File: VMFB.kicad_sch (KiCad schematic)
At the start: 112 parts, among them J1 Barrel_Jack_Switch, J10 Conn_01x03_Pin, J11 Conn_01x06_Pin, J12 Conn_01x04_Pin, J13 Conn_01x04_Pin, J14 Conn_01x04_Pin, J2 USB_B, J3 Screw_Terminal_01x02, J4 Screw_Terminal_01x03, J5 Conn_01x03_Pin, J6 Conn_01x04_Pin, J7 Conn_01x04_Pin, J8 Conn_01x04_Pin, J9 Conn_01x02_Pin, Q1 BC547, Q2 BC547, Q3 BC547, Q4 BD139, Q5 TIP41C, Q6 BC547, U1 LM358, U2 NE555P, U3 NE555P, U4 NE555P, U5 NE555P

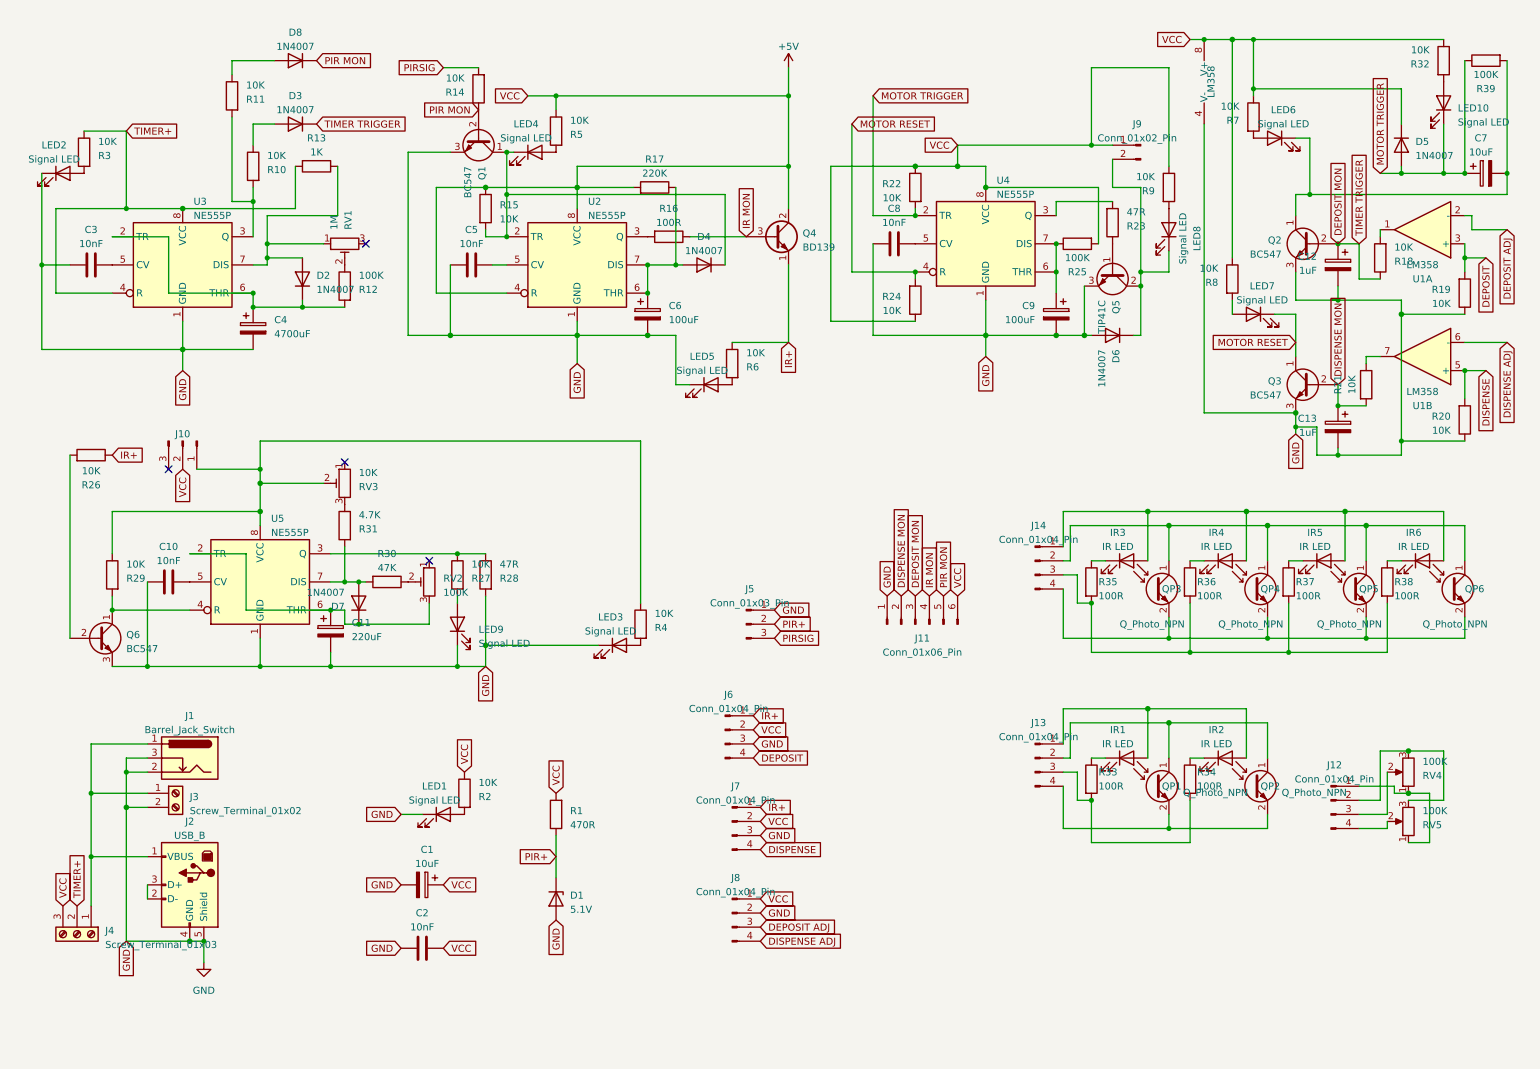
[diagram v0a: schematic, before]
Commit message: added monitoring-only header, moved IR LED switch transistor from VCC to GND and removed a pin from the sensor headers (no need for separate VCC for the IR LEDS), 100R to 47R on Q$ base, 47R to 22R on Q5 base
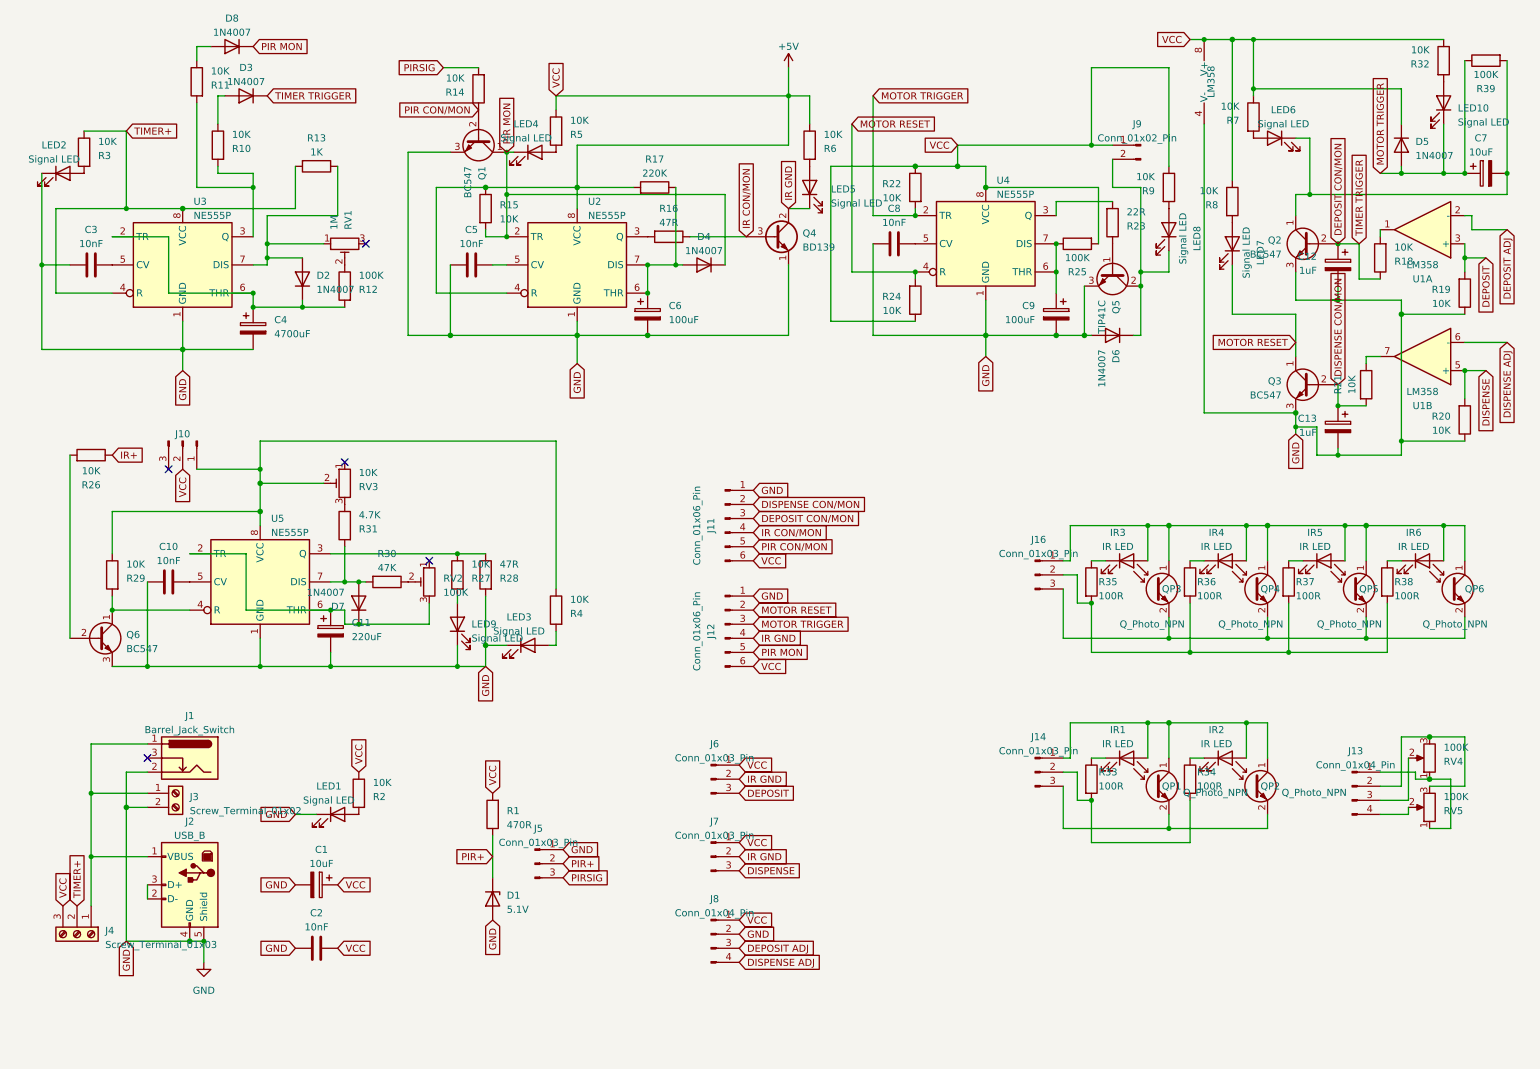
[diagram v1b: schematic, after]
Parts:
- removed J13, J14, J6, J7: Conn_01x04_Pin, Connector_PinHeader_2.54mm:PinHeader_1x04_P2.54mm_Vertical, symbol Connector:Conn_01x04_Pin
- added J12: Conn_01x06_Pin, Connector_PinHeader_2.54mm:PinHeader_1x06_P2.54mm_Vertical, symbol Connector:Conn_01x06_Pin
- added J14, J16, J6, J7: Conn_01x03_Pin, Connector_PinHeader_2.54mm:PinHeader_1x03_P2.54mm_Vertical, symbol Connector:Conn_01x03_Pin
- R16: value 100R -> 47R; footprint Resistor_THT:R_Axial_DIN0207_L6.3mm_D2.5mm_P2.54mm_Vertical -> Resistor_THT:R_Axial_DIN0309_L9.0mm_D3.2mm_P2.54mm_Vertical
- R23: value 47R -> 22R
- renumbered J12 to J13
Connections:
- net +5V: now also R6.1, J12.6 (Pin_6), J6.1 (Pin_1), J7.1 (Pin_1); no longer Q4.2 (C)
- net DEPOSIT: now also J6.3 (Pin_3)
- net DISPENSE: now also J7.3 (Pin_3)
- net GND: now also Q4.1 (E), J12.1 (Pin_1); no longer J1.3, LED5.1 (K)
- net IR+: no longer Q4.1 (E), R6.1
- net MOTOR RESET: now also J12.2 (Pin_2)
- net MOTOR TRIGGER: now also J12.3 (Pin_3)
- net PIR MON: now also D4.1 (K), LED4.1 (K), Q1.1 (C), R15.2, U2.2 (TR), J12.5 (Pin_5); no longer J11.5 (Pin_5), Q1.2 (B), R14.1
- net at IR1.2 (A), IR2.2 (A): now also QP1.1 (C), QP2.1 (C), J14.1 (Pin_1)
- net at IR3.2 (A), IR4.2 (A), IR5.2 (A)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: now also QP3.1 (C), QP4.1 (C), QP5.1 (C), QP6.1 (C), J16.1 (Pin_1)
- net at R35.2, R36.2, R37.2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: now also J16.2 (Pin_2)
- net at QP3.2 (E), QP4.2 (E), QP5.2 (E)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: now also J16.3 (Pin_3)
- net at R33.2, R34.2: now also J14.2 (Pin_2)
- net at QP1.2 (E), QP2.2 (E): now also J14.3 (Pin_3)
- net DEPOSIT MON renamed DEPOSIT CON/MON
- net DISPENSE MON renamed DISPENSE CON/MON
- net IR MON renamed IR CON/MON
- new net IR GND: J12.4 (Pin_4), J6.2 (Pin_2), J7.2 (Pin_2), LED5.1 (K), Q4.2 (C)
- new net PIR CON/MON: J11.5 (Pin_5), Q1.2 (B), R14.1
- no-connect marks 4 -> 5
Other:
- moved on the sheet: C1, C2, D1, D3, D8, J11, J13, J5, J8, LED1, LED3, LED7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

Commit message: moved dispense monitoring directly to the collector of Q2 so you can tell if it's jammed
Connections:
- net IR+ is gone; now on net IR CON/MON: R26.1
- net MOTOR TRIGGER: no longer J12.3 (Pin_3)
- net DEPOSIT MON: now reaches C7.2, LED6.1 (K), Q2.1 (C), R39.2
- net DEPOSIT MON: now also J12.3 (Pin_3)
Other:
- moved on the sheet: J10
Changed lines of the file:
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@@
   )
   (no_connect (at 87.63 111.76))
-  (no_connect (at 40.64 95.25))
+  (no_connect (at 48.26 95.25))
   (no_connect (at 72.39 93.98))
   (no_connect (at 36.83 147.32))
@@
     (stroke (width 0) (type default))
   )
-  (wire (pts (xy 45.72 95.25) (xy 57.15 95.25))
+  (wire (pts (xy 53.34 95.25) (xy 57.15 95.25))
     (stroke (width 0) (type default) (color 221 119 0 1))
   )
@@
     )
   )
-  (global_label "MOTOR TRIGGER" (shape input) (at 146.05 123.19 0) (fields_autoplaced)
+  (global_label "DEPOSIT MON" (shape input) (at 146.05 123.19 0) (fields_autoplaced)
     (effects (font (size 1.27 1.27)) (justify left))
-    (property "Intersheetrefs" "${INTERSHEET_REFS}" (at 164.0748 123.19 0) (show_name)
+    (property "Intersheetrefs" "${INTERSHEET_REFS}" (at 161.8372 123.19 0) (show_name)
       (effects (font (size 1.27 1.27)) (justify left) hide)
     )
@@
     )
   )
-  (global_label "VCC" (shape input) (at 43.18 95.25 270) (fields_autoplaced)
+  (global_label "VCC" (shape input) (at 50.8 95.25 270) (fields_autoplaced)
     (effects (font (size 1.27 1.27)) (justify right))
-    (property "Intersheetrefs" "${INTERSHEET_REFS}" (at 43.18 101.7844 90) (show_name)
+    (property "Intersheetrefs" "${INTERSHEET_REFS}" (at 50.8 101.7844 90) (show_name)
       (effects (font (size 1.27 1.27)) (justify right) hide)
     )
@@
     )
   )
+  (global_label "DEPOSIT MON" (shape input) (at 243.84 45.72 180) (fields_autoplaced)
+    (effects (font (size 1.27 1.27)) (justify right))
+    (property "Intersheetrefs" "${INTERSHEET_REFS}" (at 228.0528 45.72 0) (show_name)
+      (effects (font (size 1.27 1.27)) (justify right) hide)
+    )
+  )
   (global_label "MOTOR RESET" (shape input) (at 243.84 72.39 180) (fields_autoplaced)
     (effects (font (size 1.27 1.27)) (justify right))
@@
     )
   )
-  (global_label "IR+" (shape input) (at 30.48 92.71 0) (fields_autoplaced)
+  (global_label "IR CON{slash}MON" (shape input) (at 30.48 92.71 0) (fields_autoplaced)
     (effects (font (size 1.27 1.27)) (justify left))
-    (property "Intersheetrefs" "${INTERSHEET_REFS}" (at 36.833 92.71 0) (show_name)
+    (property "Intersheetrefs" "${INTERSHEET_REFS}" (at 45.6021 92.71 0) (show_name)
       (effects (font (size 1.27 1.27)) (justify left) hide)
     )
@@
     )
   )
-  (symbol (lib_id "Connector:Conn_01x03_Pin") (at 43.18 90.17 270) (unit 1)
+  (symbol (lib_id "Connector:Conn_01x03_Pin") (at 50.8 90.17 270) (unit 1)
     (in_bom yes) (on_board yes) (dnp no) (fields_autoplaced)
-    (property "Reference" "J10" (at 43.18 88.9 90)
+    (property "Reference" "J10" (at 50.8 88.9 90)
       (effects (font (size 1.27 1.27)))
     )
-    (property "Value" "Conn_01x03_Pin" (at 46.99 90.805 0)
+    (property "Value" "Conn_01x03_Pin" (at 54.61 90.805 0)
       (effects (font (size 1.27 1.27)) hide)
     )
-    (property "Footprint" "Connector_PinHeader_2.54mm:PinHeader_1x03_P2.54mm_Vertical" (at 43.18 90.17 0)
+    (property "Footprint" "Connector_PinHeader_2.54mm:PinHeader_1x03_P2.54mm_Vertical" (at 50.8 90.17 0)
       (effects (font (size 1.27 1.27)) hide)
     )
-    (property "Datasheet" "~" (at 43.18 90.17 0)
+    (property "Datasheet" "~" (at 50.8 90.17 0)
       (effects (font (size 1.27 1.27)) hide)
     )

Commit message: updated version to 1.3
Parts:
- Q1, Q2, Q3, Q6: footprint Package_TO_SOT_THT:TO-92_Inline -> Package_TO_SOT_THT:TO-92_Inline_Wide
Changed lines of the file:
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@@
       (effects (font (size 1.27 1.27)) (justify left))
     )
-    (property "Footprint" "Package_TO_SOT_THT:TO-92_Inline" (at 33.02 127.635 0)
+    (property "Footprint" "Package_TO_SOT_THT:TO-92_Inline_Wide" (at 33.02 127.635 0)
       (effects (font (size 1.27 1.27) italic) (justify left) hide)
     )
@@
       (effects (font (size 1.27 1.27)) (justify left))
     )
-    (property "Footprint" "Package_TO_SOT_THT:TO-92_Inline" (at 94.615 40.64 0)
+    (property "Footprint" "Package_TO_SOT_THT:TO-92_Inline_Wide" (at 94.615 40.64 0)
       (effects (font (size 1.27 1.27) italic) (justify left) hide)
     )
@@
       (effects (font (size 1.27 1.27)) (justify left))
     )
-    (property "Footprint" "Package_TO_SOT_THT:TO-92_Inline" (at 241.3 81.915 0)
+    (property "Footprint" "Package_TO_SOT_THT:TO-92_Inline_Wide" (at 241.3 81.915 0)
       (effects (font (size 1.27 1.27) italic) (justify left) hide)
     )
@@
       (effects (font (size 1.27 1.27)) (justify left))
     )
-    (property "Footprint" "Package_TO_SOT_THT:TO-92_Inline" (at 241.3 56.515 0)
+    (property "Footprint" "Package_TO_SOT_THT:TO-92_Inline_Wide" (at 241.3 56.515 0)
       (effects (font (size 1.27 1.27) italic) (justify left) hide)
     )

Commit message: added LDR-based light sensor to turn off timed dispense when the sun sets
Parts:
- added J16, J17: Conn_01x03_Pin, Connector_PinHeader_2.54mm:PinHeader_1x03_P2.54mm_Vertical, symbol Connector:Conn_01x03_Pin
- added LDR1: GL5549, OptoDevice:R_LDR_5.1x4.3mm_P3.4mm_Vertical, symbol Sensor_Optical:LDR07
- added R41: 470, Resistor_THT:R_Axial_DIN0207_L6.3mm_D2.5mm_P2.54mm_Vertical, symbol Device:R
- added RV6: 25K, Potentiometer_THT:Potentiometer_Piher_PT-10-V10_Vertical, symbol Device:R_Potentiometer
- renumbered J16 to J15
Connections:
- net GND: now also J17.3 (Pin_3)
- net TIMER+: now also J17.1 (Pin_1); no longer U3.4 (R)
- new net: J16.1 (Pin_1), R41.1
- new net: LDR1.1, R41.2
- new net: J17.2 (Pin_2), U3.4 (R)
- new net: J16.2 (Pin_2), LDR1.2, RV6.2
- new net: J16.3 (Pin_3), RV6.3
- no-connect marks 5 -> 6

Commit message: improvements to the daytimer, and added an LED so you can see the status
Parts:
- removed J16: Conn_01x03_Pin, Connector_PinHeader_2.54mm:PinHeader_1x03_P2.54mm_Vertical, symbol Connector:Conn_01x03_Pin
- added J18: Conn_01x02_Pin, Connector_PinHeader_2.54mm:PinHeader_1x02_P2.54mm_Vertical, symbol Connector:Conn_01x02_Pin
- added LED11: Signal LED, LED_THT:LED_D5.0mm, symbol Device:LED
- added Q7: BC547, Package_TO_SOT_THT:TO-92_Inline_Wide, symbol Transistor_BJT:BC547
- added R40, R42: 10K, Resistor_THT:R_Axial_DIN0207_L6.3mm_D2.5mm_P2.54mm_Vertical, symbol Device:R
- R12: value 100K -> 220K
- RV1: value 1M -> 2M
- RV6: value 25K -> 10K
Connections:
- net GND: now also RV6.3, Q7.3 (E)
- net TIMER+: now also R40.2, R42.1
- net at R41.1: now also J18.1 (Pin_1)
- net at U3.4 (R): now also LED11.1 (K), Q7.1 (C), R40.1; no longer J17.2 (Pin_2)
- net at RV6.2: now also J17.2 (Pin_2), Q7.2 (B); no longer LDR1.2
- new net: J18.2 (Pin_2), LDR1.2
- new net: LED11.2 (A), R42.2
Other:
- moved on the sheet: J17

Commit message: minor adjustments to the daytimer
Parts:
- added R43: 470R, Resistor_THT:R_Axial_DIN0207_L6.3mm_D2.5mm_P2.54mm_Vertical, symbol Device:R
- R40: value 10K -> 22K
- RV6: value 10K -> 25K
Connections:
- net at J17.2 (Pin_2), Q7.2 (B): now also R43.1; no longer RV6.2
- new net: R43.2, RV6.2
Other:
- moved on the sheet: RV6
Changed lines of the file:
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@@
   (junction (at 246.38 45.72) (diameter 0) (color 0 0 0 0)
   )
-  (junction (at 29.21 83.82) (diameter 0) (color 0 0 0 0)
-  )
   (junction (at 200.66 54.61) (diameter 0) (color 0 0 0 0)
   )
@@
   (junction (at 242.57 128.27) (diameter 0) (color 0 0 0 1)
   )
+  (junction (at 35.56 83.82) (diameter 0) (color 0 0 0 0)
+  )
   (junction (at 224.79 128.27) (diameter 0) (color 0 0 0 1)
   )
+  (junction (at 21.59 80.01) (diameter 0) (color 0 0 0 0)
+  )
   (junction (at 200.66 59.69) (diameter 0) (color 0 0 0 0)
   )
@@
   (junction (at 238.76 125.73) (diameter 0) (color 0 255 0 1)
   )
-  (junction (at 25.4 80.01) (diameter 0) (color 0 0 0 0)
-  )
   (junction (at 92.71 110.49) (diameter 0) (color 0 0 0 0)
   )
@@
   (no_connect (at 87.63 111.76))
   (no_connect (at 48.26 95.25))
-  (no_connect (at 29.21 76.2))
+  (no_connect (at 35.56 76.2))
   (no_connect (at 72.39 93.98))
   (no_connect (at 36.83 147.32))
@@
     (stroke (width 0) (type default))
   )
-  (wire (pts (xy 20.32 81.28) (xy 25.4 81.28))
+  (wire (pts (xy 20.32 81.28) (xy 21.59 81.28))
     (stroke (width 0) (type default))
   )
@@
     (stroke (width 0) (type default) (color 194 0 0 1))
   )
+  (wire (pts (xy 35.56 83.82) (xy 29.21 83.82))
+    (stroke (width 0) (type default))
+  )
   (wire (pts (xy 236.22 17.78) (xy 236.22 26.67))
     (stroke (width 0) (type default) (color 194 0 0 1))
@@
     (stroke (width 0) (type default))
   )
-  (wire (pts (xy 29.21 83.82) (xy 39.37 83.82))
-    (stroke (width 0) (type default))
-  )
   (wire (pts (xy 191.77 129.54) (xy 191.77 132.08))
     (stroke (width 0) (type default))
@@
     (stroke (width 0) (type default) (color 0 0 0 1))
   )
+  (wire (pts (xy 21.59 80.01) (xy 21.59 81.28))
+    (stroke (width 0) (type default))
+  )
   (wire (pts (xy 251.46 91.44) (xy 251.46 92.71))
     (stroke (width 0) (type default))
@@
     (stroke (width 0) (type default))
   )
+  (wire (pts (xy 35.56 83.82) (xy 39.37 83.82))
+    (stroke (width 0) (type default))
+  )
   (wire (pts (xy 55.88 41.91) (xy 55.88 44.45))
     (stroke (width 0) (type default))
@@
     (stroke (width 0) (type default))
   )
-  (wire (pts (xy 25.4 81.28) (xy 25.4 80.01))
-    (stroke (width 0) (type default))
-  )
   (wire (pts (xy 243.84 87.63) (xy 243.84 88.9))
     (stroke (width 0) (type default) (color 0 0 0 1))
@@
     (stroke (width 0) (type default) (color 255 0 0 1))
   )
-  (wire (pts (xy 25.4 73.66) (xy 25.4 80.01))
+  (wire (pts (xy 21.59 73.66) (xy 21.59 80.01))
     (stroke (width 0) (type default))
   )
@@
     (stroke (width 0) (type default))
   )
-  (wire (pts (xy 31.75 73.66) (xy 25.4 73.66))
+  (wire (pts (xy 31.75 73.66) (xy 21.59 73.66))
     (stroke (width 0) (type default))
   )
@@
     (stroke (width 0) (type default) (color 0 0 0 1))
   )
+  (wire (pts (xy 21.59 80.01) (xy 24.13 80.01))
+    (stroke (width 0) (type default))
+  )
   (wire (pts (xy 110.49 90.17) (xy 110.49 116.84))
     (stroke (width 0) (type default) (color 221 119 0 1))
@@
       (effects (font (size 1.27 1.27)) (justify right))
     )
-    (property "Value" "10K" (at 22.86 65.405 0)
+    (property "Value" "22K" (at 22.86 65.405 0)
       (effects (font (size 1.27 1.27)) (justify right))
     )
@@
     )
   )
-  (symbol (lib_id "Device:R_Potentiometer") (at 29.21 80.01 0) (mirror y) (unit 1)
+  (symbol (lib_id "Device:R_Potentiometer") (at 35.56 80.01 0) (mirror y) (unit 1)
     (in_bom yes) (on_board yes) (dnp no)
-    (property "Reference" "RV6" (at 33.02 80.01 90)
+    (property "Reference" "RV6" (at 39.37 80.01 90)
       (effects (font (size 1.27 1.27)))
     )
-    (property "Value" "10K" (at 35.56 80.01 90)
+    (property "Value" "25K" (at 41.91 80.01 90)
       (effects (font (size 1.27 1.27)))
     )
-    (property "Footprint" "Potentiometer_THT:Potentiometer_Piher_PT-10-V10_Vertical" (at 29.21 80.01 0)
+    (property "Footprint" "Potentiometer_THT:Potentiometer_Piher_PT-10-V10_Vertical" (at 35.56 80.01 0)
       (effects (font (size 1.27 1.27)) hide)
     )
-    (property "Datasheet" "~" (at 29.21 80.01 0)
+    (property "Datasheet" "~" (at 35.56 80.01 0)
       (effects (font (size 1.27 1.27)) hide)
     )
@@
         )
       )
+    )
+  )
+  (symbol (lib_id "Device:R") (at 27.94 80.01 90) (unit 1)
+    (in_bom yes) (on_board yes) (dnp no)
+    (property "Reference" "R43" (at 28.575 82.55 0)
+      (effects (font (size 1.27 1.27)) (justify right))
+    )
+    (property "Value" "470R" (at 26.035 82.55 0)
+      (effects (font (size 1.27 1.27)) (justify right))
+    )
+    (property "Footprint" "Resistor_THT:R_Axial_DIN0207_L6.3mm_D2.5mm_P2.54mm_Vertical" (at 27.94 81.788 90)
+      (effects (font (size 1.27 1.27)) hide)
+    )
+    (property "Datasheet" "~" (at 27.94 80.01 0)
+      (effects (font (size 1.27 1.27)) hide)
+    )
+    (pin "1")
+    (pin "2")
+    (instances
+      (project "VMFB"
+        (path "/840789ee-60d4-4003-8113-c1b030a45492"
+          (reference "R43") (unit 1)
+        )
+      )

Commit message: more adjustments to the daytimer
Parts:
- removed J13, J8: Conn_01x04_Pin, Connector_PinHeader_2.54mm:PinHeader_1x04_P2.54mm_Vertical, symbol Connector:Conn_01x04_Pin
- RV4, RV5: footprint Potentiometer_THT:Potentiometer_Piher_T-16H_Single_Horizontal -> Potentiometer_THT:Potentiometer_Piher_PT-10-V10_Vertical
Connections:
- net +5V: now also R32.2, RV4.3, RV5.1; no longer R32.1
- net DEPOSIT ADJ: now also RV4.2
- net DISPENSE ADJ: now also RV5.2
- net GND: now also J17.2 (Pin_2), RV4.1, RV5.3; no longer J17.3 (Pin_3), RV6.3
- net TIMER+: now also RV6.1; no longer J17.1 (Pin_1)
- net at LED10.2 (A): now also R32.1; no longer R32.2
- net at R41.1: now also LDR1.2; no longer J18.1 (Pin_1)
- net at R41.2: now also J18.1 (Pin_1); no longer LDR1.1
- net at Q7.2 (B), R43.1: now also J17.3 (Pin_3); no longer J17.2 (Pin_2)
- net at J18.2 (Pin_2): now also LDR1.1; no longer LDR1.2
- no-connect marks 6 -> 7
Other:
- moved on the sheet: R40, R41, R42, R43, RV4, RV5, RV6
